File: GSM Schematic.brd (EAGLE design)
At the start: 100 x 80 mm, 19 parts, among them IC1 7805T, J1 5.5x2.1mm Barrel, J2 AVR_SPI_PRG_62X3_LOCK, Q2 16M, U1 ATMEGA328P-PU

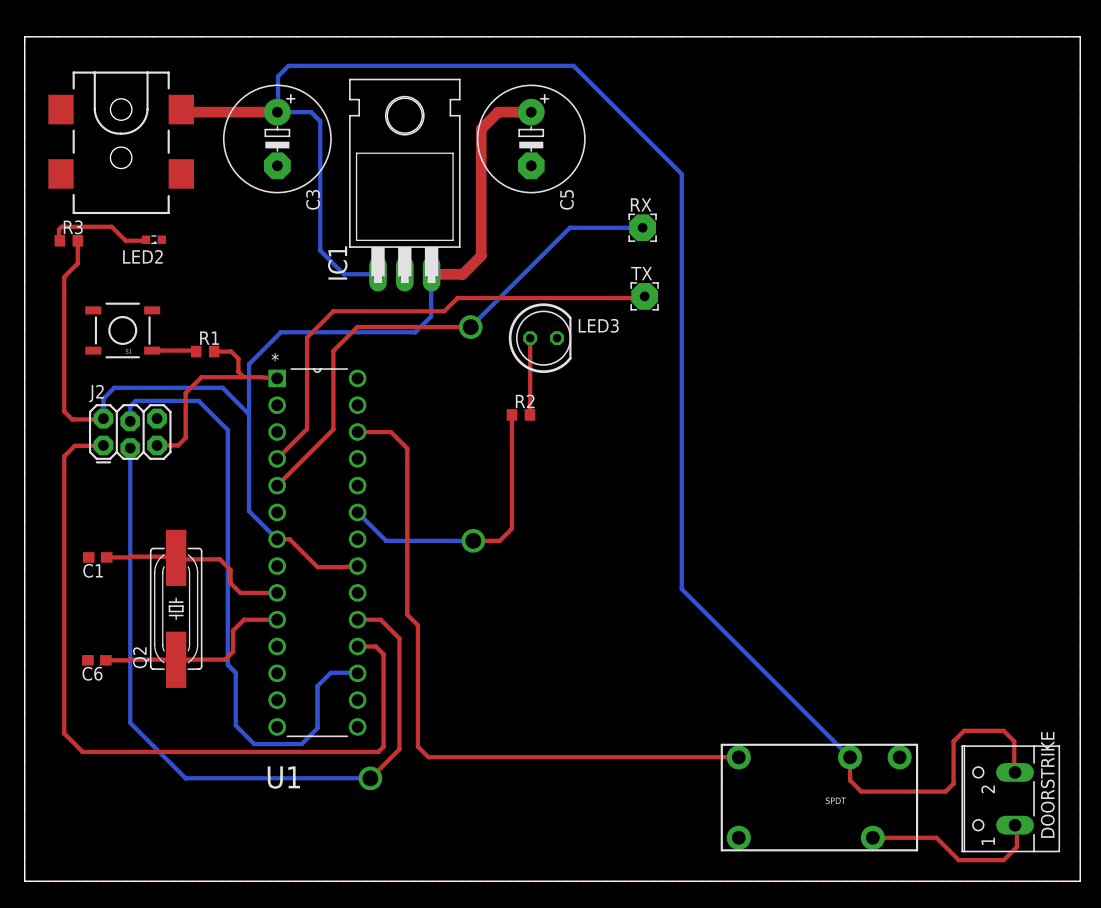
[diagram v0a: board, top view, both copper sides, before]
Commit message: updated the Schematic and changed PCB layout
Updated the Schematic and included a surface mount for the Voltage regulator and changed the layout of the PCB and added a logo to it
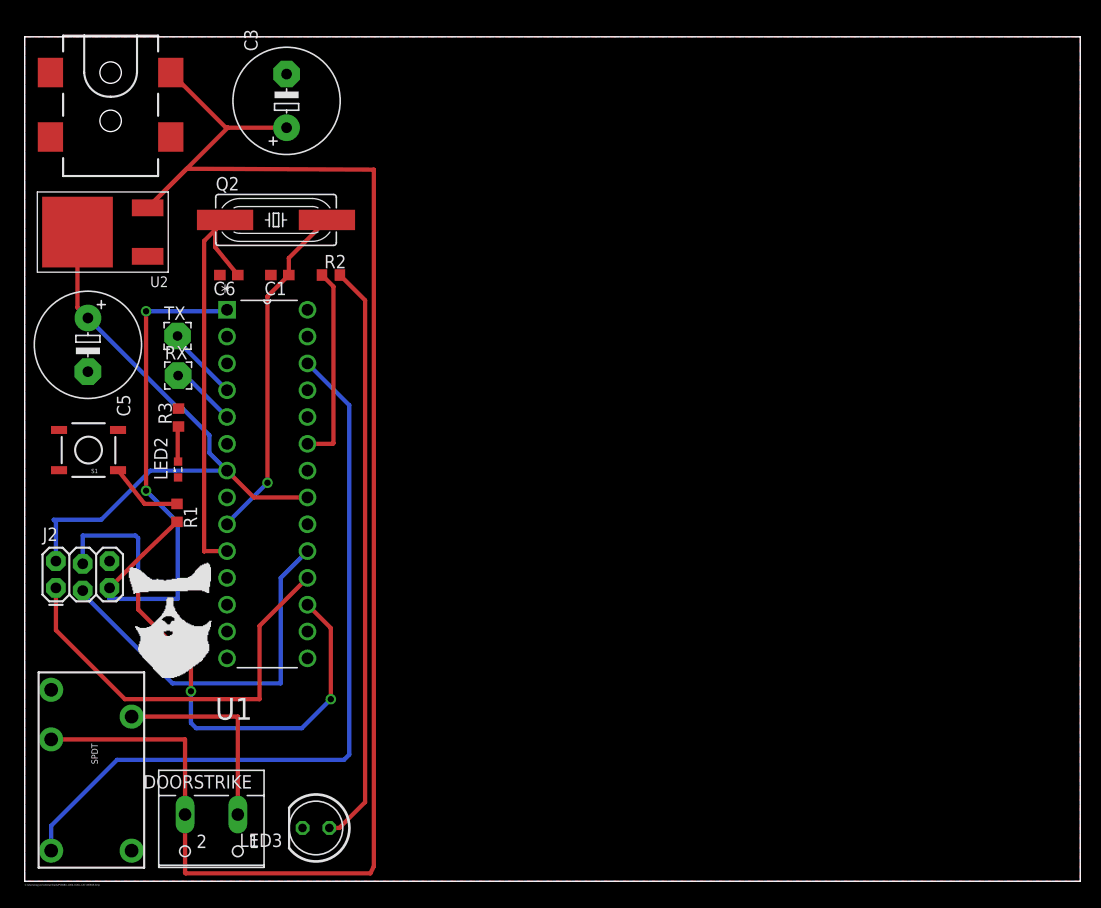
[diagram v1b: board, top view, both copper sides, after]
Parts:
- removed IC1: 7805T, linear:TO220H
- added U2: LM317MDT-TR, MF_IC_Power:TO-252-3
- moved DOORSTRIKE 74.9 mm to (17.7, 5.05), turned to 180 degrees
- moved SPDT 70.3 mm to (6.32, 11.8), turned to 0 degrees
- moved LED3 51.2 mm to (27.6, 5.05), turned to 180 degrees
- moved C5 46.3 mm to (5.99, 50.8)
- moved RX 46.2 mm to (14.5, 47.9)
- moved TX 44.4 mm to (14.5, 51.7)
- moved C6 38.6 mm to (19.3, 57.4)
- moved Q2 38.0 mm to (23.8, 62.6), turned to 0 degrees
- moved C1 31.8 mm to (24.2, 57.4)
- moved R2 22.4 mm to (29.0, 57.4)
- moved LED2 21.9 mm to (14.5, 39.0), turned to 90 degrees
- moved R3 19.7 mm to (14.6, 43.9), turned to 90 degrees
- moved R1 15.5 mm to (14.4, 34.9), turned to 270 degrees
- moved J2 14.2 mm to (2.96, 27.8)
- moved S1 11.8 mm to (6.05, 40.8)
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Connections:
- net 12V: now also U2.2; no longer IC1.1
- net 5V: now also U2.PAD; no longer IC1.3
- net GND: now also U2.1; no longer IC1.2
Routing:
- net 5V: track 110.4 -> 59.7 mm
- net N$6: track 7.28 -> 55.3 mm
- net N$12: track 49.1 -> 6.26 mm, vias 1 -> 0
- net N$1: track 46.3 -> 7.08 mm
- net N$5: track 70.0 -> 36.1 mm, vias 1 -> 0
- net N$8: track 73.1 -> 39.4 mm
- net N$10: track 21.0 -> 52.7 mm, vias 0 -> 2
- net N$18: track 19.0 -> 39.4 mm
- net N$16: track 18.3 -> 32.8 mm, vias 0 -> 1
- net 12V: track 166.8 -> 156.5 mm
- net N$3: track 10.0 -> 0.00 mm
- net N$9: track 27.0 -> 18.9 mm, vias 1 -> 0
- net N$14: track 64.8 -> 72.1 mm
- net N$7: track 57.8 -> 52.1 mm, vias 0 -> 3
- net N$11: track 0.00 -> 3.25 mm
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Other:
- board text added: "C:/Users/rayyachx/Downloads/PCB/BU-1004-COOL-CAT-WEB16.bmp"

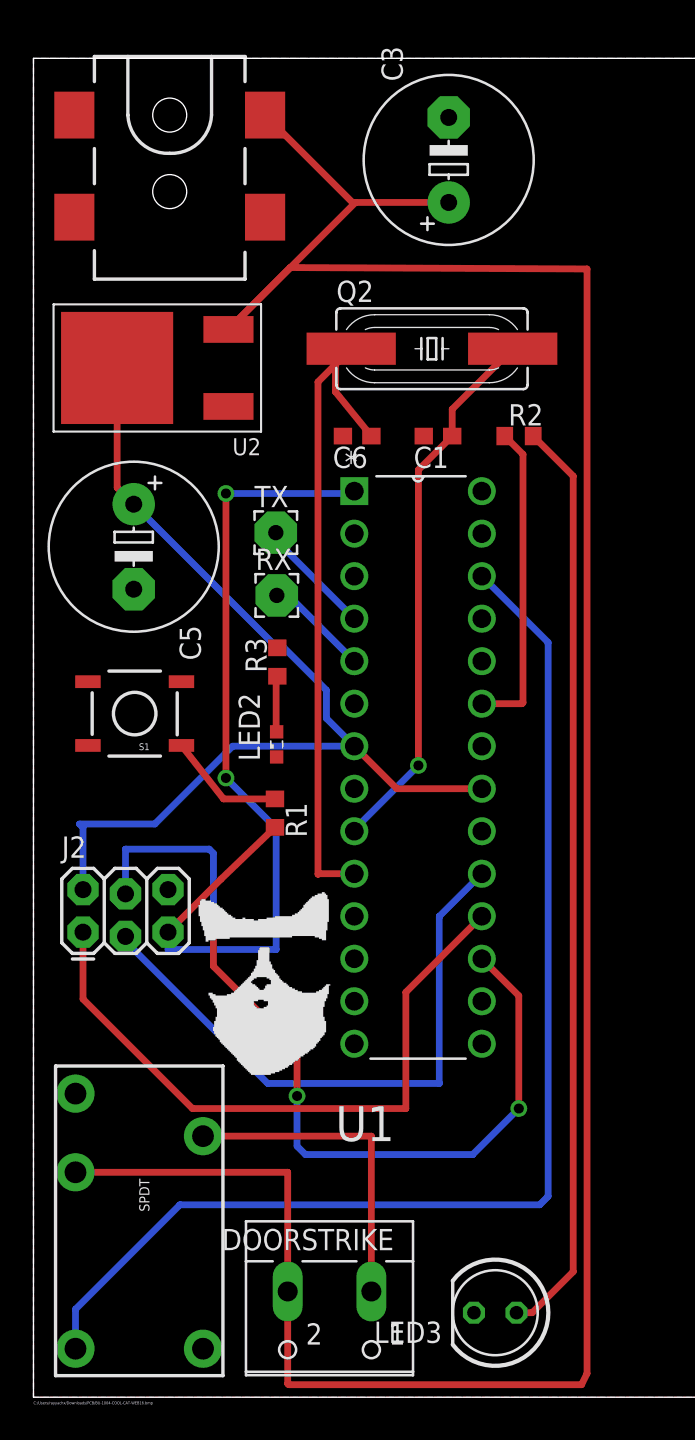
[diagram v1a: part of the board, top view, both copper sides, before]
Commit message: Changed the logo location and added Revision #
DRC errors down to 49 (All of the errors are Stop Errors)
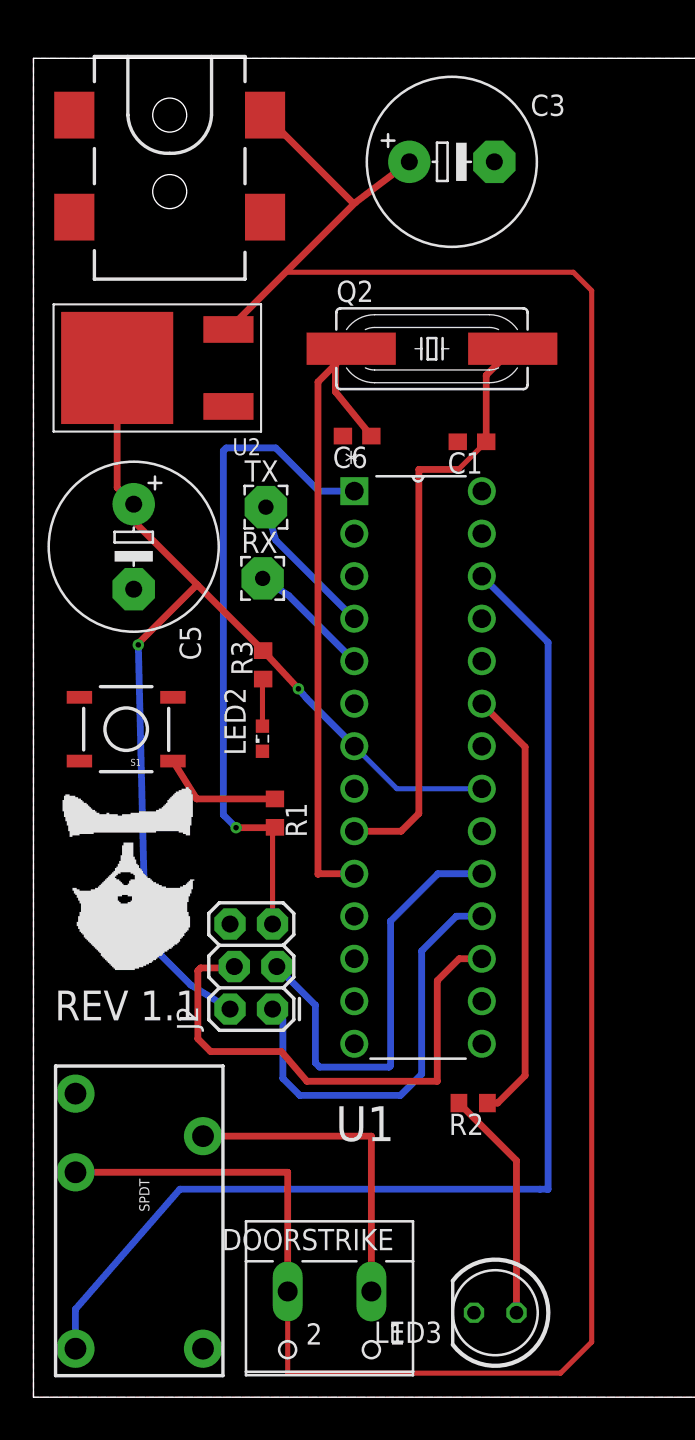
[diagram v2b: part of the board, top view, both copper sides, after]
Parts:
- J2: value AVR_SPI_PRG_62X3_LOCK -> AVR_SPI
- moved R2 39.9 mm to (26.3, 17.6), turned to 180 degrees
- moved J2 12.2 mm to (14.3, 23.2), turned to 90 degrees
- moved C1 2.06 mm to (26.2, 57.1)
- moved TX 1.64 mm to (13.9, 53.2)
- moved RX 1.32 mm to (13.7, 48.9)
- moved S1 1.06 mm to (5.54, 39.9)
- moved LED2 0.91 mm to (13.7, 39.3)
- moved R3 0.86 mm to (13.7, 43.8)
- moved C3 0.22 mm to (25.0, 73.8), turned to 0 degrees
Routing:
- net N$6: track 55.3 -> 14.0 mm
- net N$7: track 52.1 -> 31.0 mm, vias 3 -> 0
- net N$8: track 39.4 -> 25.5 mm
- net N$10: track 52.7 -> 40.0 mm, vias 2 -> 1
- net N$5: track 36.1 -> 26.6 mm
- net N$9: track 18.9 -> 26.2 mm
- net 5V: track 59.7 -> 66.3 mm, vias 0 -> 2
- net 12V: track 156.5 -> 152.3 mm
- net N$11: track 3.25 -> 0.00 mm
- net N$16: track 32.8 -> 35.8 mm, vias 1 -> 0
- net N$3: track 0.00 -> 2.83 mm
- net N$1: track 7.08 -> 8.69 mm
- net N$12: track 6.26 -> 7.41 mm
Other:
- board text added: "REV 1.1"
- board text removed: "C:/Users/rayyachx/Downloads/PCB/BU-1004-COOL-CAT-WEB16.bmp"

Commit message: Arranged names for components
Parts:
- ATMEGA328P-PU: value ATMEGA328P-PU -> (none)
- AVR_SPI: value AVR_SPI -> (none)
- renumbered DOORSTRIKE to DRSTRIKE, J2 to AVR_SPI, U1 to ATMEGA328P-PU
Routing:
- net 12V: track 152.3 -> 144.3 mm
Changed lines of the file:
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@@
 </class>
 </classes>
-<designrules name="OSH-Park-2-layer *">
+<designrules name="OSH-Park-2-layer">
 <description language="de">&lt;b&gt;EAGLE Design Rules&lt;/b&gt;
 &lt;p&gt;
@@
 <param name="mdPadVia" value="6mil"/>
 <param name="mdViaVia" value="6mil"/>
-<param name="mdSmdPad" value="0mil"/>
-<param name="mdSmdVia" value="0mil"/>
-<param name="mdSmdSmd" value="0mil"/>
+<param name="mdSmdPad" value="6mil"/>
+<param name="mdSmdVia" value="6mil"/>
+<param name="mdSmdSmd" value="6mil"/>
 <param name="mdViaViaSameLayer" value="8mil"/>
 <param name="mnLayersViaInSmd" value="2"/>
@@
 <element name="C5" library="rcl" package="E5-10,5" value="10u" x="5.99" y="50.82" rot="R270"/>
 <element name="C6" library="rcl" package="C0603" value="22p" x="19.34" y="57.43" rot="R180"/>
-<element name="DOORSTRIKE" library="con-wago-500" package="W237-102" value="" x="17.69" y="5.05" rot="R180">
+<element name="DRSTRIKE" library="con-wago-500" package="W237-102" value="" x="17.69" y="5.05" rot="R180">
 <attribute name="MF" value="" x="17.69" y="5.05" size="1.778" layer="27" rot="R180" display="off"/>
 <attribute name="MPN" value="237-102" x="17.69" y="5.05" size="1.778" layer="27" rot="R180" display="off"/>
@@
 <attribute name="PROD_ID" value="CONN-08106" x="8.14" y="76.61" size="1.778" layer="27" rot="R270" display="off"/>
 </element>
-<element name="J2" library="SparkFun-Connectors" package="2X3_LOCK" value="AVR_SPI" x="14.285125" y="23.193309375" rot="R90"/>
+<element name="AVR_SPI" library="SparkFun-Connectors" package="2X3_LOCK" value="" x="14.285125" y="23.193309375" smashed="yes" rot="R90">
+<attribute name="NAME" x="17.54401875" y="22.26194375" size="1.27" layer="25" ratio="10" rot="R90"/>
+<attribute name="VALUE" x="17.460125" y="21.923309375" size="1.27" layer="27" rot="R90"/>
+</element>
 <element name="LED2" library="led" package="SML0603" value="" x="13.683425" y="39.348634375" rot="R90"/>
 <element name="LED3" library="led" package="LED5MM" value="" x="27.59" y="5.05" rot="R180"/>
@@
 <element name="SPDT" library="SparkFun-Electromechanical" package="RELAY-JZC" value="RELAYPTH4" x="6.32" y="11.79"/>
 <element name="TX" library="wirepad" package="2,54/0,9" value="" x="13.88739375" y="53.18385"/>
-<element name="U1" library="Atmel_By_element14_Batch_1-00" package="DIP254P762X457-28" value="ATMEGA328P-PU" x="26.79" y="21.12">
+<element name="ATMEGA328P-PU" library="Atmel_By_element14_Batch_1-00" package="DIP254P762X457-28" value="" x="26.79" y="21.12" smashed="yes">
 <attribute name="MPN" value="ATMEGA328P-PU" x="26.79" y="21.12" size="1.778" layer="27" display="off"/>
 <attribute name="OC_NEWARK" value="15R0268" x="26.79" y="21.12" size="1.778" layer="27" display="off"/>
@@
 <attribute name="SUPPLIER" value="Atmel" x="26.79" y="21.12" size="1.778" layer="27" display="off"/>
 <attribute name="OC_FARNELL" value="1715487" x="26.79" y="21.12" size="1.778" layer="27" display="off"/>
+<attribute name="NAME" x="31.258609375" y="25.079028125" size="2.0828" layer="25" ratio="10" rot="SR90"/>
+<attribute name="VALUE" x="19.5256" y="57.315" size="2.0828" layer="27" ratio="10" rot="SR0"/>
 </element>
 <element name="U2" library="MF_IC_Power" package="TO-252-3" value="LM317MDT-TR" x="5" y="61.5" rot="R180">
@@
 <contactref element="LED2" pad="C"/>
 <contactref element="C3" pad="-"/>
-<contactref element="U1" pad="8"/>
-<contactref element="U1" pad="22"/>
-<contactref element="J2" pad="6"/>
+<contactref element="ATMEGA328P-PU" pad="8"/>
+<contactref element="ATMEGA328P-PU" pad="22"/>
+<contactref element="AVR_SPI" pad="6"/>
 <contactref element="S1" pad="3"/>
 <contactref element="J1" pad="P$4"/>
@@
 </signal>
 <signal name="N$7">
-<contactref element="J2" pad="4"/>
-<contactref element="U1" pad="17"/>
+<contactref element="AVR_SPI" pad="4"/>
+<contactref element="ATMEGA328P-PU" pad="17"/>
 <wire x1="26.79" y1="26.2" x2="25.438078125" y2="26.2" width="0.4064" layer="1"/>
 <wire x1="25.438078125" y1="26.2" x2="24.1275875" y2="24.889509375" width="0.4064" layer="1"/>
@@
 </signal>
 <signal name="N$8">
-<contactref element="U1" pad="18"/>
-<contactref element="J2" pad="1"/>
+<contactref element="ATMEGA328P-PU" pad="18"/>
+<contactref element="AVR_SPI" pad="1"/>
 <wire x1="26.79" y1="28.74" x2="25.2690125" y2="28.74" width="0.4064" layer="16"/>
 <wire x1="25.2690125" y1="28.74" x2="23.196346875" y2="26.667334375" width="0.4064" layer="16"/>
@@
 </signal>
 <signal name="N$10">
-<contactref element="U1" pad="1"/>
-<contactref element="J2" pad="5"/>
+<contactref element="ATMEGA328P-PU" pad="1"/>
+<contactref element="AVR_SPI" pad="5"/>
 <contactref element="R1" pad="2"/>
 <wire x1="14.43" y1="34.05" x2="14.285125" y2="33.905125" width="0.3048" layer="1"/>
@@
 </signal>
 <signal name="5V">
-<contactref element="U1" pad="20"/>
+<contactref element="ATMEGA328P-PU" pad="20"/>
 <contactref element="R3" pad="2"/>
-<contactref element="J2" pad="2"/>
-<contactref element="U1" pad="21"/>
+<contactref element="AVR_SPI" pad="2"/>
+<contactref element="ATMEGA328P-PU" pad="21"/>
 <contactref element="C5" pad="+"/>
-<contactref element="U1" pad="7"/>
+<contactref element="ATMEGA328P-PU" pad="7"/>
 <contactref element="U2" pad="PAD"/>
 <wire x1="5" y1="61.5" x2="5" y2="54.35" width="0.4064" layer="1"/>
@@
 </signal>
 <signal name="N$1">
-<contactref element="U1" pad="4"/>
+<contactref element="ATMEGA328P-PU" pad="4"/>
 <contactref element="TX" pad="1"/>
 <wire x1="19.17" y1="46.52" x2="14.48" y2="51.21" width="0.4064" layer="16"/>
@@
 </signal>
 <signal name="N$12">
-<contactref element="U1" pad="5"/>
+<contactref element="ATMEGA328P-PU" pad="5"/>
 <contactref element="RX" pad="1"/>
 <wire x1="19.17" y1="43.98" x2="15.24" y2="47.91" width="0.4064" layer="16"/>
@@
 </signal>
 <signal name="N$14">
-<contactref element="U1" pad="26"/>
+<contactref element="ATMEGA328P-PU" pad="26"/>
 <contactref element="SPDT" pad="5"/>
 <wire x1="2.51" y1="2.9" x2="2.51" y2="5.26" width="0.4064" layer="16"/>
@@
 <contactref element="J1" pad="VIN0"/>
 <contactref element="SPDT" pad="2"/>
-<contactref element="DOORSTRIKE" pad="2"/>
+<contactref element="DRSTRIKE" pad="2"/>
 <contactref element="C3" pad="+"/>
 <contactref element="U2" pad="2"/>
@@
 <wire x1="13.84" y1="76.61" x2="19.06" y2="71.39" width="0.4064" layer="1"/>
 <wire x1="19.06" y1="71.39" x2="19.24" y2="71.39" width="0.4064" layer="1"/>
-<wire x1="11.65" y1="63.8" x2="19.24" y2="71.39" width="0.4064" layer="1"/>
-<wire x1="11.65" y1="63.8" x2="15.068609375" y2="67.218609375" width="0.3048" layer="1"/>
-<wire x1="15.068609375" y1="67.218609375" x2="32.254775" y2="67.218609375" width="0.3048" layer="1"/>
-<wire x1="32.254775" y1="67.218609375" x2="33.35533125" y2="66.118053125" width="0.3048" layer="1"/>
-<wire x1="33.35533125" y1="66.118053125" x2="33.35533125" y2="3.30166875" width="0.3048" layer="1"/>
-<wire x1="33.35533125" y1="3.30166875" x2="31.492853125" y2="1.439190625" width="0.3048" layer="1"/>
-<wire x1="31.492853125" y1="1.439190625" x2="15.238475" y2="1.439190625" width="0.3048" layer="1"/>
-<wire x1="15.238475" y1="1.439190625" x2="15.19" y2="1.487665625" width="0.3048" layer="1"/>
-<wire x1="15.19" y1="1.487665625" x2="15.19" y2="6.32" width="0.3048" layer="1"/>
+<wire x1="11.65" y1="63.8" x2="15.8731375" y2="68.0231375" width="0.4064" layer="1"/>
+<wire x1="15.8731375" y1="68.0231375" x2="19.24" y2="71.39" width="0.4064" layer="1"/>
 <wire x1="19.24" y1="71.39" x2="22.457559375" y2="73.816803125" width="0.4064" layer="1"/>
+<wire x1="15.19" y1="6.32" x2="15.19" y2="3.7734375" width="0.4064" layer="1"/>
+<wire x1="15.19" y1="3.7734375" x2="17.60890625" y2="1.35453125" width="0.4064" layer="1"/>
+<wire x1="17.60890625" y1="1.35453125" x2="31.238875" y2="1.35453125" width="0.4064" layer="1"/>
+<wire x1="31.238875" y1="1.35453125" x2="32.59340625" y2="2.7090625" width="0.4064" layer="1"/>
+<wire x1="32.59340625" y1="2.7090625" x2="32.59340625" y2="65.61010625" width="0.4064" layer="1"/>
+<wire x1="32.59340625" y1="65.61010625" x2="30.180375" y2="68.0231375" width="0.4064" layer="1"/>
+<wire x1="30.180375" y1="68.0231375" x2="15.8731375" y2="68.0231375" width="0.4064" layer="1"/>
 </signal>
 <signal name="N$16">
 <contactref element="C1" pad="1"/>
 <contactref element="Q2" pad="2"/>
-<contactref element="U1" pad="9"/>
+<contactref element="ATMEGA328P-PU" pad="9"/>
 <wire x1="23.02703125" y1="55.43703125" x2="23.02703125" y2="34.879178125" width="0.4064" layer="1"/>
 <wire x1="23.02703125" y1="34.879178125" x2="21.967853125" y2="33.82" width="0.4064" layer="1"/>
@@
 <contactref element="C6" pad="1"/>
 <contactref element="Q2" pad="1"/>
-<contactref element="U1" pad="10"/>
+<contactref element="ATMEGA328P-PU" pad="10"/>
 <wire x1="18.984" y1="62.65" x2="18.042" y2="61.708" width="0.4064" layer="1"/>
 <wire x1="18.042" y1="61.708" x2="17" y2="60.666" width="0.4064" layer="1"/>
@@
 </signal>
 <signal name="N$5">
-<contactref element="U1" pad="19"/>
-<contactref element="J2" pad="3"/>
+<contactref element="ATMEGA328P-PU" pad="19"/>
+<contactref element="AVR_SPI" pad="3"/>
 <wire x1="26.79" y1="31.28" x2="24.168709375" y2="31.28" width="0.4064" layer="16"/>
 <wire x1="24.168709375" y1="31.28" x2="21.333865625" y2="28.44515625" width="0.4064" layer="16"/>
@@
 <signal name="N$4">
 <contactref element="SPDT" pad="4"/>
-<contactref element="DOORSTRIKE" pad="1"/>
+<contactref element="DRSTRIKE" pad="1"/>
 <wire x1="10.13" y1="15.6" x2="20.19" y2="15.6" width="0.4064" layer="1"/>
 <wire x1="20.19" y1="15.6" x2="20.19" y2="6.32" width="0.4064" layer="1"/>
@@
 <signal name="N$9">
 <contactref element="R2" pad="1"/>
-<contactref element="U1" pad="23"/>
+<contactref element="ATMEGA328P-PU" pad="23"/>
 <wire x1="27.12180625" y1="17.5771625" x2="27.736146875" y2="17.5771625" width="0.4064" layer="1"/>
 <wire x1="27.736146875" y1="17.5771625" x2="29.376396875" y2="19.2174125" width="0.4064" layer="1"/>
